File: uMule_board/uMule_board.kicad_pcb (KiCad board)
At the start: 2 copper layers, 140 x 140 mm, 148 parts, among them J1 12V IN, J10 Conn_01x04, J11 Conn_01x04, J12 Conn_01x04, J13 Conn_01x04, J14 Conn_01x04, J2 Dynamixel, J3 Li-Dar_UART, J4 ESP32_UART, J5 Conn_ST_STDC14, J6 I2C, J7 SPI_IMU, J8 Conn_02x04_Odd_Even, J9 Conn_02x04_Odd_Even, P1 BPV10NF, P2 BPV10NF, P3 BPV10NF, P4 BPV10NF, P5 BPV10NF, P6 BPV10NF, P7 BPV10NF, P8 BPV10NF, Q1 AON6407, Q2 S9015, SW1 DBG_BUTT, SW2 RST, U1 TPS62933, U10 OPA397DBVR, U11 OPA397DBVR, U12 OPA397DBVR, U13 OPA397DBVR, U14 OPA397DBVR, U15 OPA397DBVR, U16 SP3485CN, U2 TLV761, U3 LM431BMC3, U4 INA219AxD, U5 TPS62933, U6 STM32F103RCTx, U7 FM24C64B, U8 OPA397DBVR, U9 OPA397DBVR, Y1 8MHz

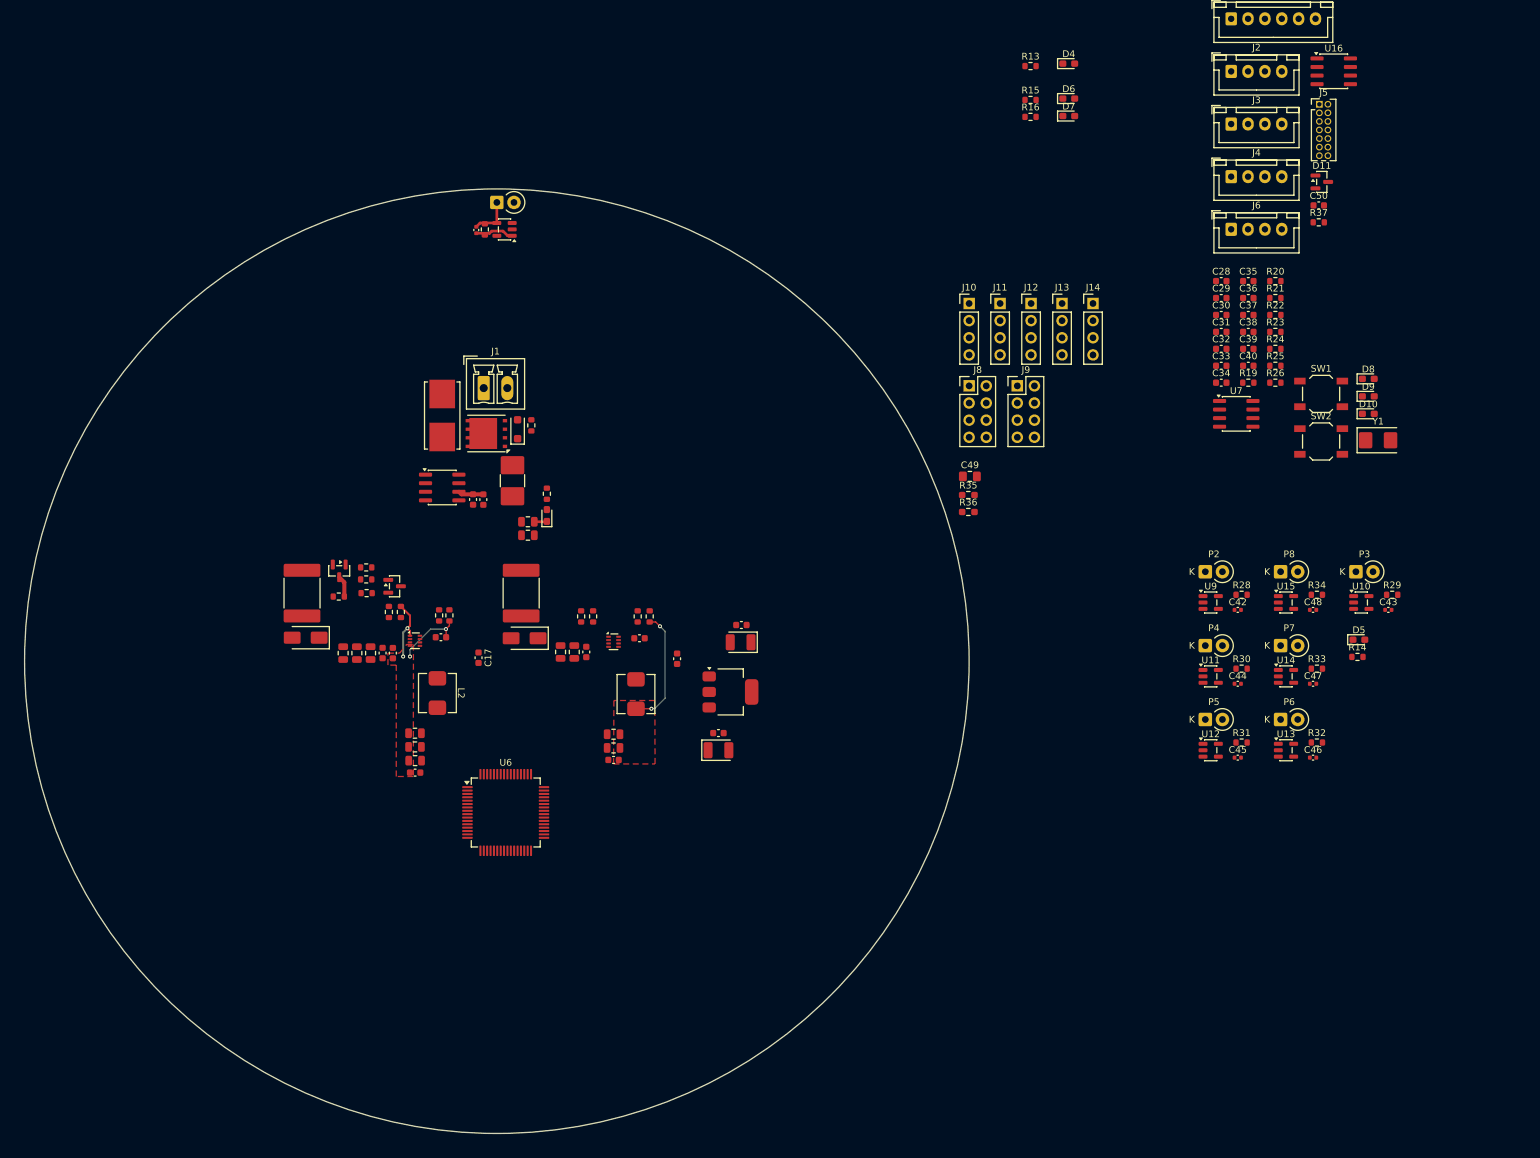
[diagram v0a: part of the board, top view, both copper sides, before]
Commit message: after placing photodiodes
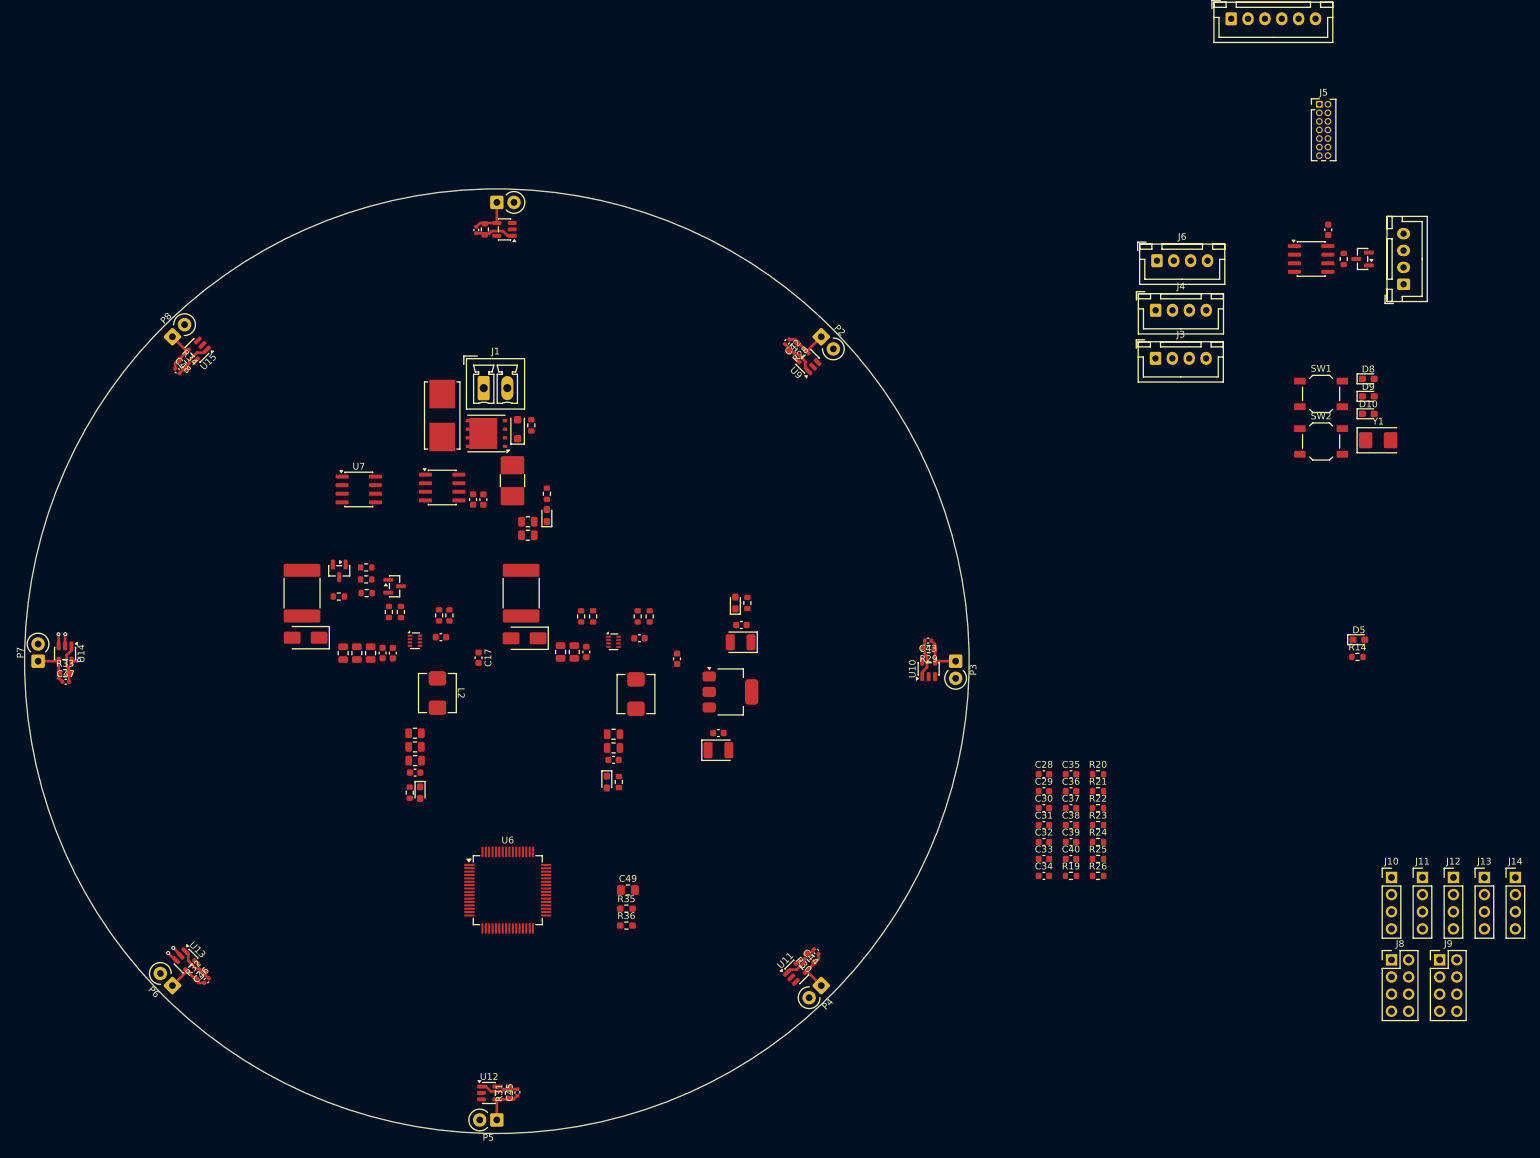
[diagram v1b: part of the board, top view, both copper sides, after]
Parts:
- moved R33 185.5 mm to (64.0, 117.0)
- moved C47 184.9 mm to (64.1, 118.3)
- moved P7 184.2 mm to (60.0, 115.2), turned to 90 degrees
- moved U14 181.0 mm to (64.0, 114.1), turned to -90 degrees
- moved C48 172.0 mm to (80.6, 72.2), turned to -45 degrees
- moved R34 171.5 mm to (81.5, 71.2), turned to -45 degrees
- moved R32 169.1 mm to (84.0, 161.8), turned to 45 degrees
- moved P6 168.9 mm to (79.9, 163.3), turned to 135 degrees
- moved P8 167.9 mm to (79.9, 67.2), turned to 45 degrees
- moved C46 167.3 mm to (84.9, 162.6), turned to 45 degrees
- moved U13 166.0 mm to (81.9, 159.7), turned to -45 degrees
- moved U15 165.7 mm to (83.5, 69.2), turned to -135 degrees
- moved D4 144.6 mm to (116.6, 134.7), turned to -90 degrees
- moved R13 141.7 mm to (115.1, 134.7), turned to 90 degrees
- moved U7 130.5 mm to (107.5, 89.8)
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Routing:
- net -5V: track 19.9 -> 3.34 mm, vias 4 -> 2
- net +5V: track 17.7 -> 1.20 mm, vias 2 -> 1
- net GND: track 8.85 -> 0.00 mm
- net Net-(P5-K): track 0.00 -> 6.33 mm
- net Net-(P7-K): track 0.00 -> 6.33 mm
- net Net-(P3-K): track 0.00 -> 6.33 mm
- net Net-(P2-K): track 0.00 -> 6.33 mm
- net Net-(P8-K): track 0.00 -> 6.33 mm
- net Net-(P4-K): track 0.00 -> 6.33 mm
- net Net-(P6-K): track 0.00 -> 6.33 mm
- net /Photodiodes/PHO_7: track 0.00 -> 5.75 mm
- net /Photodiodes/PHO_1: track 0.00 -> 5.75 mm
- net /Photodiodes/PHO_5: track 0.00 -> 5.75 mm
- net /Photodiodes/PHO_3: track 0.00 -> 5.75 mm
- net /Photodiodes/PHO_4: track 0.00 -> 5.75 mm
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- removed copper zone on F.Cu, net +5V
- removed copper zone on F.Cu, net -5V

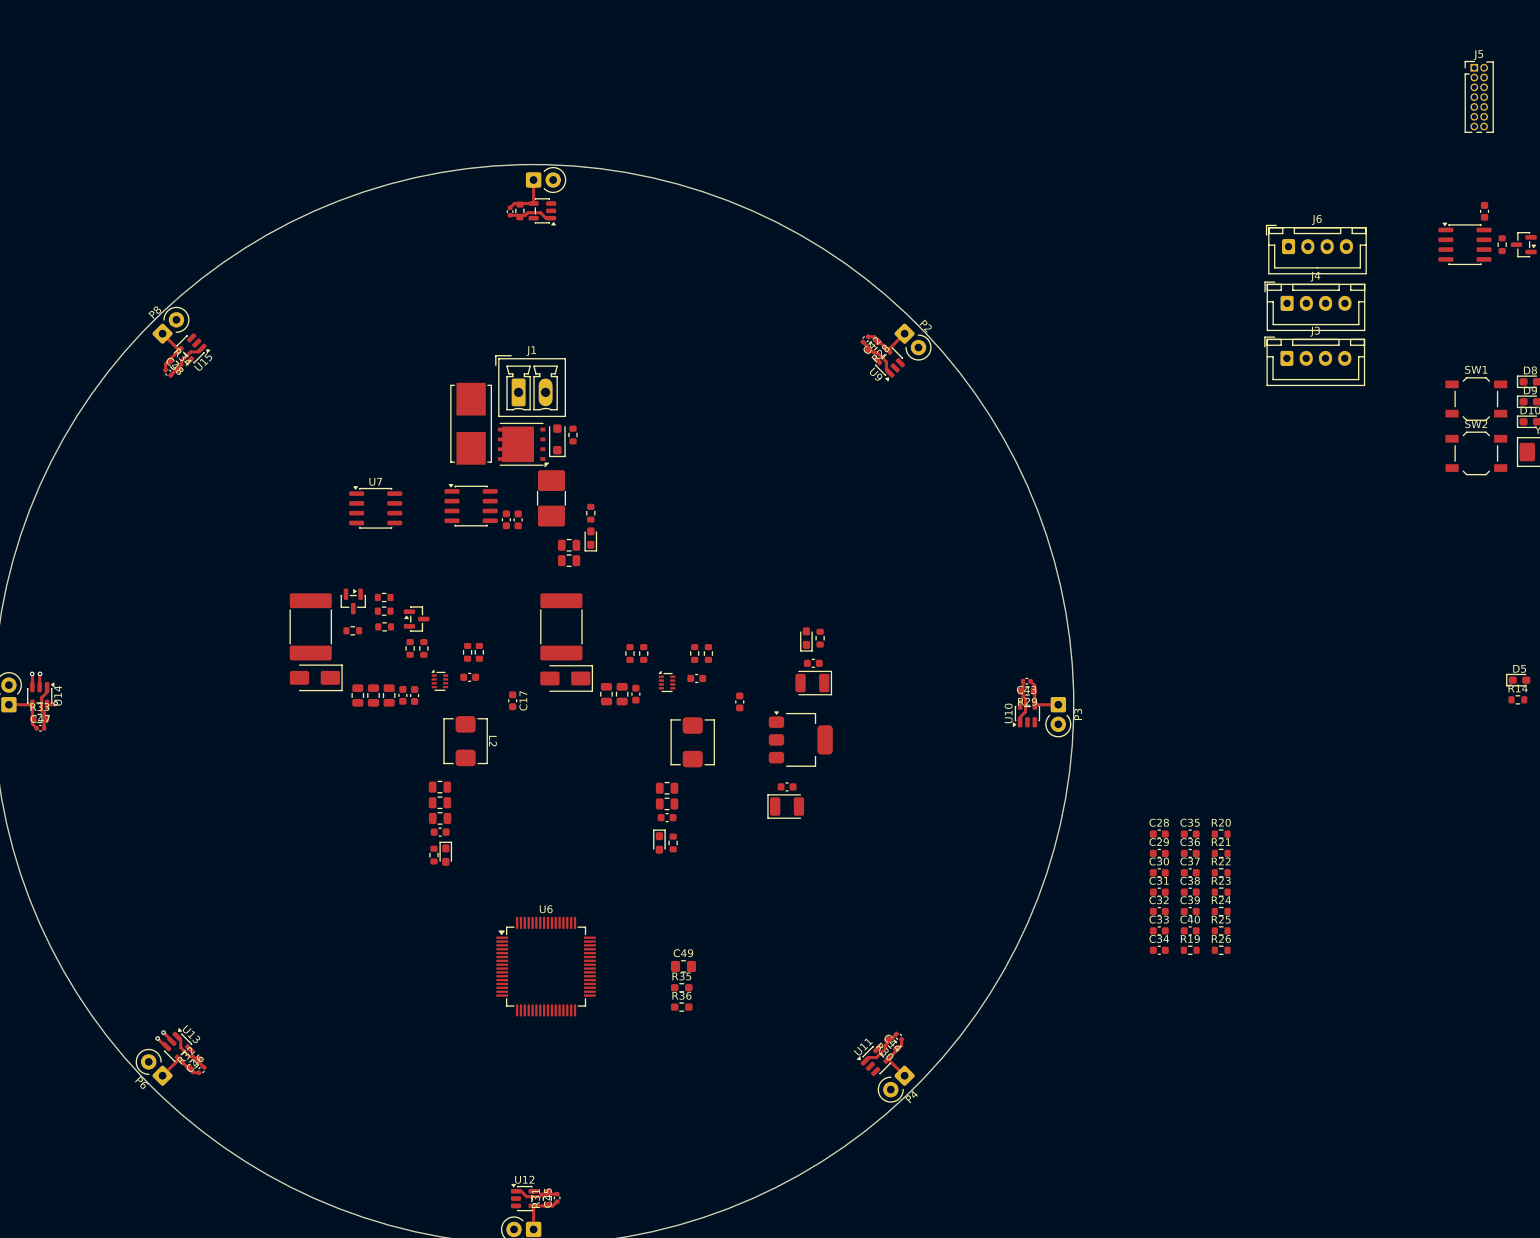
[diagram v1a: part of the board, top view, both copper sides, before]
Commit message: placed uC, initial traces connection, Matrzed trases lenghts for photodiodes (idk why)
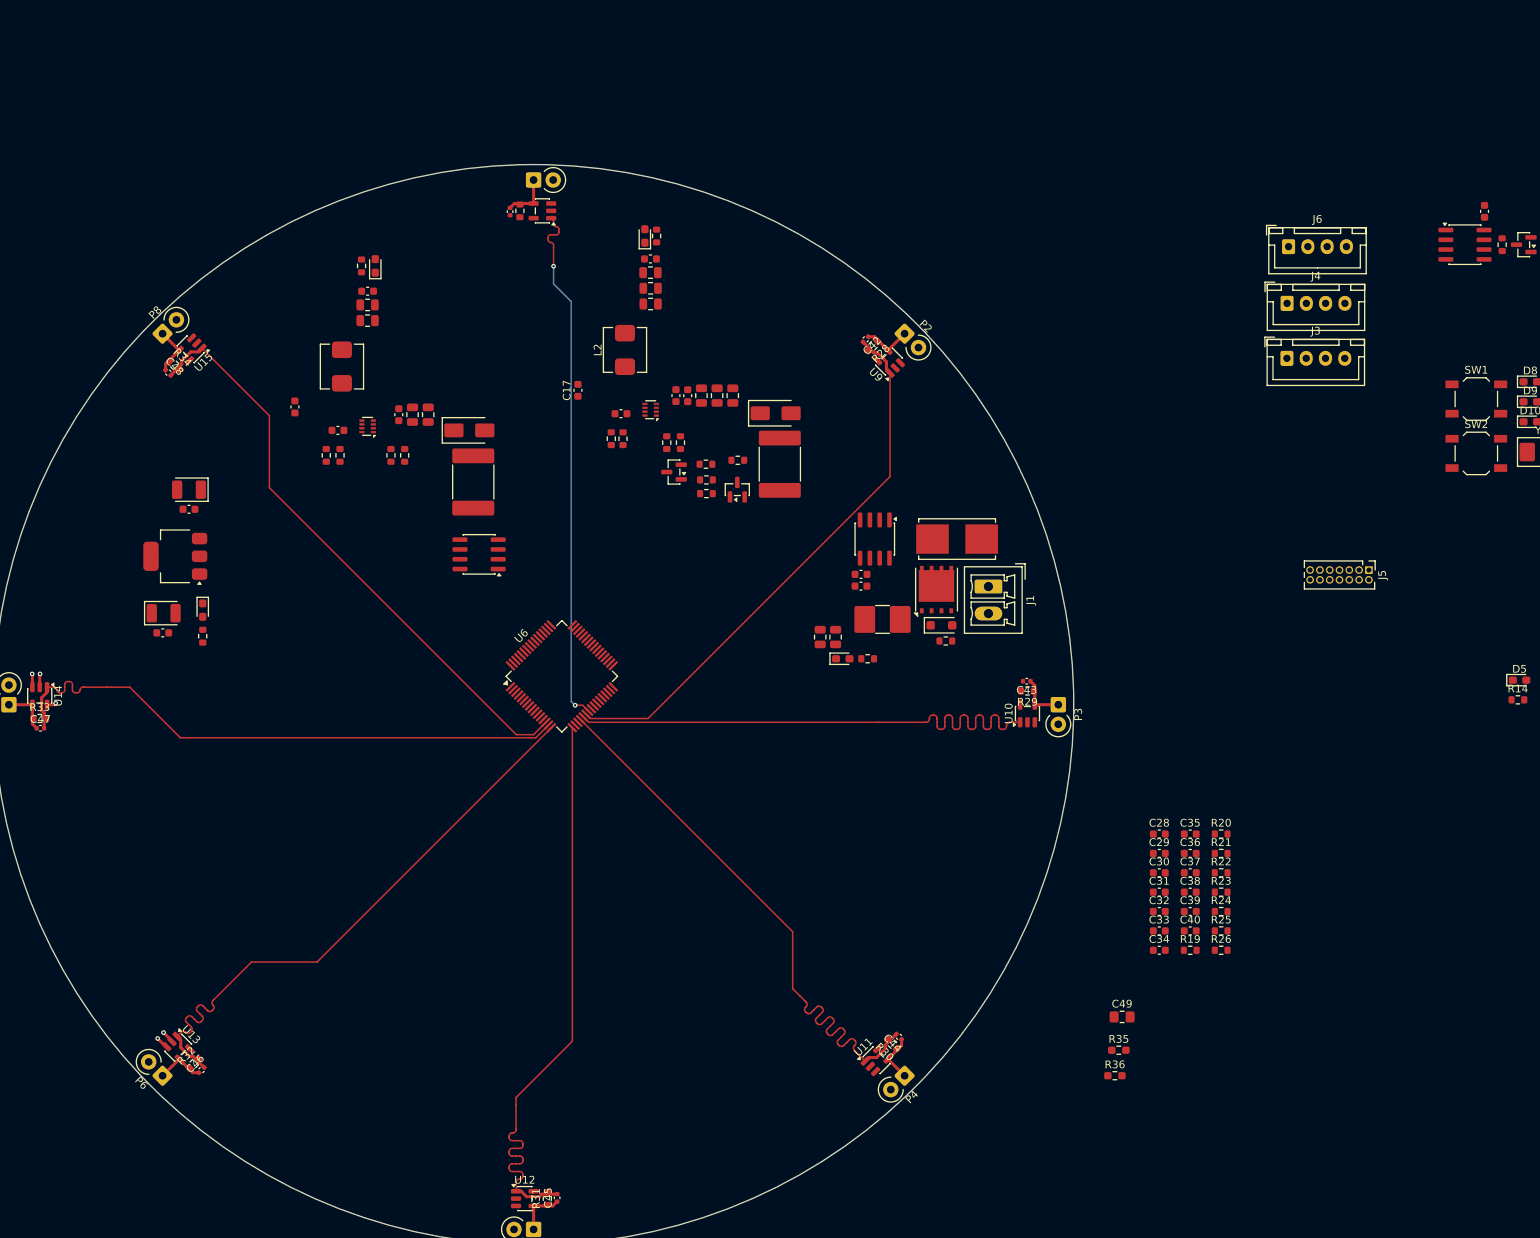
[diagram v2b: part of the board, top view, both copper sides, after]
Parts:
- moved C11 87.7 mm to (83.3, 87.4), turned to 180 degrees
- moved C12 85.4 mm to (83.3, 89.9), turned to 180 degrees
- moved R13 85.3 mm to (143.9, 54.5), turned to -90 degrees
- moved R15 85.0 mm to (105.7, 58.4), turned to 90 degrees
- moved C14 84.6 mm to (80.0, 103.4), turned to 0 degrees
- moved U2 84.5 mm to (81.5, 96.0), turned to 180 degrees
- moved C13 84.4 mm to (79.9, 105.9), turned to 0 degrees
- moved D4 84.3 mm to (142.4, 54.5), turned to 90 degrees
- moved D6 83.4 mm to (107.5, 58.4), turned to 90 degrees
- moved R16 80.0 mm to (85.1, 106.4)
- moved C23 79.1 mm to (143.1, 57.5), turned to 0 degrees
- moved C5 78.5 mm to (106.5, 61.7), turned to 0 degrees
- moved D7 78.3 mm to (85.1, 103.0), turned to -90 degrees
- moved C26 75.8 mm to (143.1, 59.2), turned to 0 degrees
- moved C6 75.4 mm to (106.5, 63.4), turned to 0 degrees
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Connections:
- U6 pad 14: /Photodiodes/PHO_0 -> /Photodiodes/PHO_7
- U6 pad 15: /Photodiodes/PHO_1 -> /Photodiodes/PHO_6
- U6 pad 16: /Photodiodes/PHO_2 -> /Photodiodes/PHO_5
- U6 pad 17: /Photodiodes/PHO_3 -> /Photodiodes/PHO_4
- U6 pad 20: /Photodiodes/PHO_4 -> /Photodiodes/PHO_3
- U6 pad 21: /Photodiodes/PHO_5 -> /Photodiodes/PHO_2
- U6 pad 22: /Photodiodes/PHO_6 -> /Photodiodes/PHO_1
- U6 pad 23: /Photodiodes/PHO_7 -> /Photodiodes/PHO_0
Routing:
- net /Photodiodes/PHO_7: track 5.75 -> 77.2 mm
- net /Photodiodes/PHO_6: track 5.75 -> 77.1 mm
- net /Photodiodes/PHO_5: track 5.75 -> 77.1 mm
- net /Photodiodes/PHO_4: track 5.75 -> 77.0 mm
- net /Photodiodes/PHO_3: track 5.75 -> 77.0 mm
- net /Photodiodes/PHO_1: track 5.75 -> 71.8 mm
- net /Photodiodes/PHO_2: track 5.75 -> 71.1 mm
- net /Photodiodes/PHO_0: track 5.75 -> 68.3 mm, vias 0 -> 2
